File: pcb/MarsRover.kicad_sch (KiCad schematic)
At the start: 13 parts, among them M1 Vibrationsmotor L, M2 Vibrationsmotor R, Q1 AO3400A, Q2 AO3400A, U1 ESP32-DevKitC V4

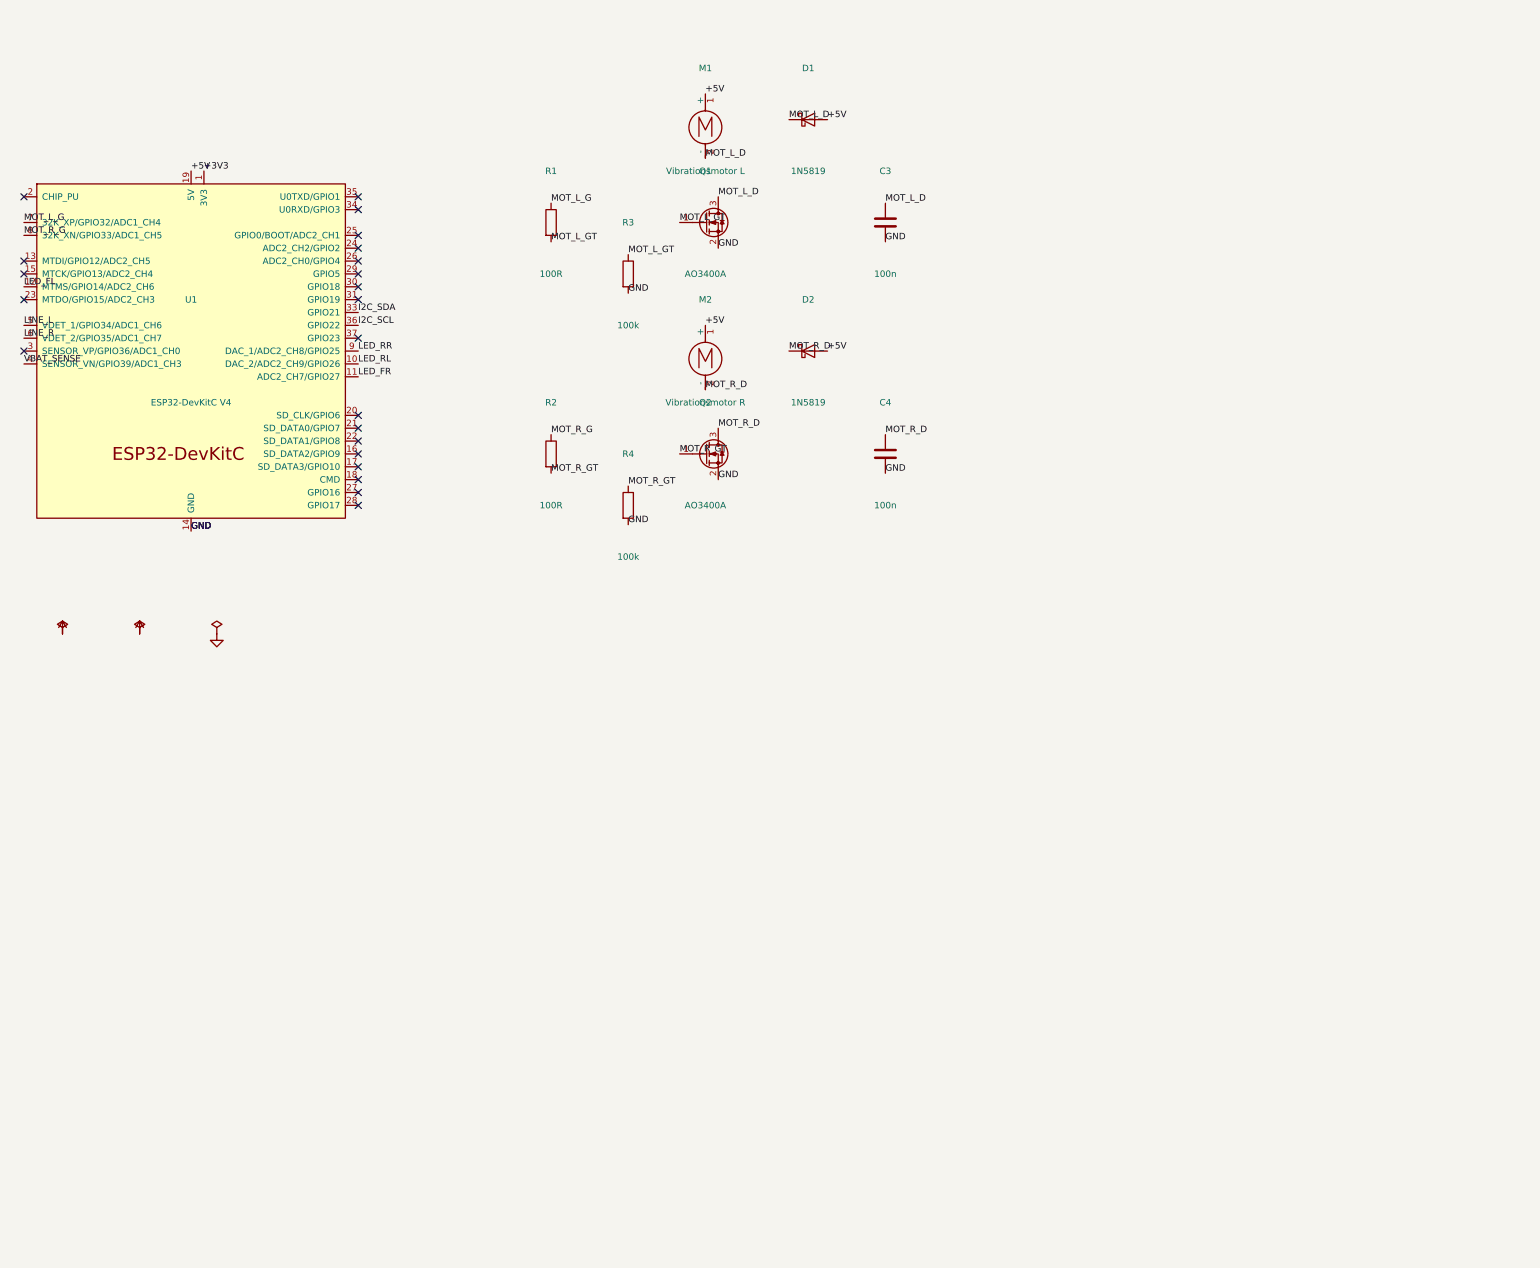
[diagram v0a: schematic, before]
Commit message: Schaltplan vollstaendig: 38 Bauteile, null ERC-Fehler
Stufe 2 ergaenzt: Liniensensoren mit Emitterfolger, vier Signal-LEDs mit
Vorwiderstaenden, beide I2C-Module als Steckverbinder, Ladeschaltung,
Schalter, Step-Up, Siebung und der optionale Spannungsteiler fuer die
Akkumessung.

106 Netzlabels, 23 Nicht-angeschlossen-Zeichen.
ERC: null Fehler, drei Warnungen, alle erklaert:
 * 2x lib_symbol_mismatch an den Dioden -- Folge des Aufloesens der
   Vererbung, kosmetisch, elektrisch ohne Wirkung
 * 1x USB_VBUS haengt allein, und das ist richtig: die USB-C-Buchse
   sitzt auf dem TP4056-Fertigmodul, nicht auf unserer Platine

Netzliste gegengeprueft: GND 29 Knoten, +5V 8, +3V3 7, I2C je 3,
die Motorzweige 4/3/2 wie entworfen.

Zur Frage nach einer interaktiven Loesung fuer den Schaltplan:
kipy bringt ein vollstaendiges schematic-Modul mit (create_items,
update_items, get_symbols, Commits), aber dessen Quelltext traegt
"versionadded: KiCad 11". Die mitgelieferten Protobuf-Definitionen sind
die von KiCad 10, daher fehlende Namen -- und die Gegenseite im
laufenden KiCad kennt die Befehle ohnehin nicht. Nicht ueberbrueckbar.
KiCad 11 wird fuer Februar 2027 erwartet; ein Wechsel hiesse Nightly,
und das Dateiformat waere eine Einbahnstrasse. Bleibt bei 10.

Co-Authored-By: Claude Opus 5 <noreply@anthropic.com>
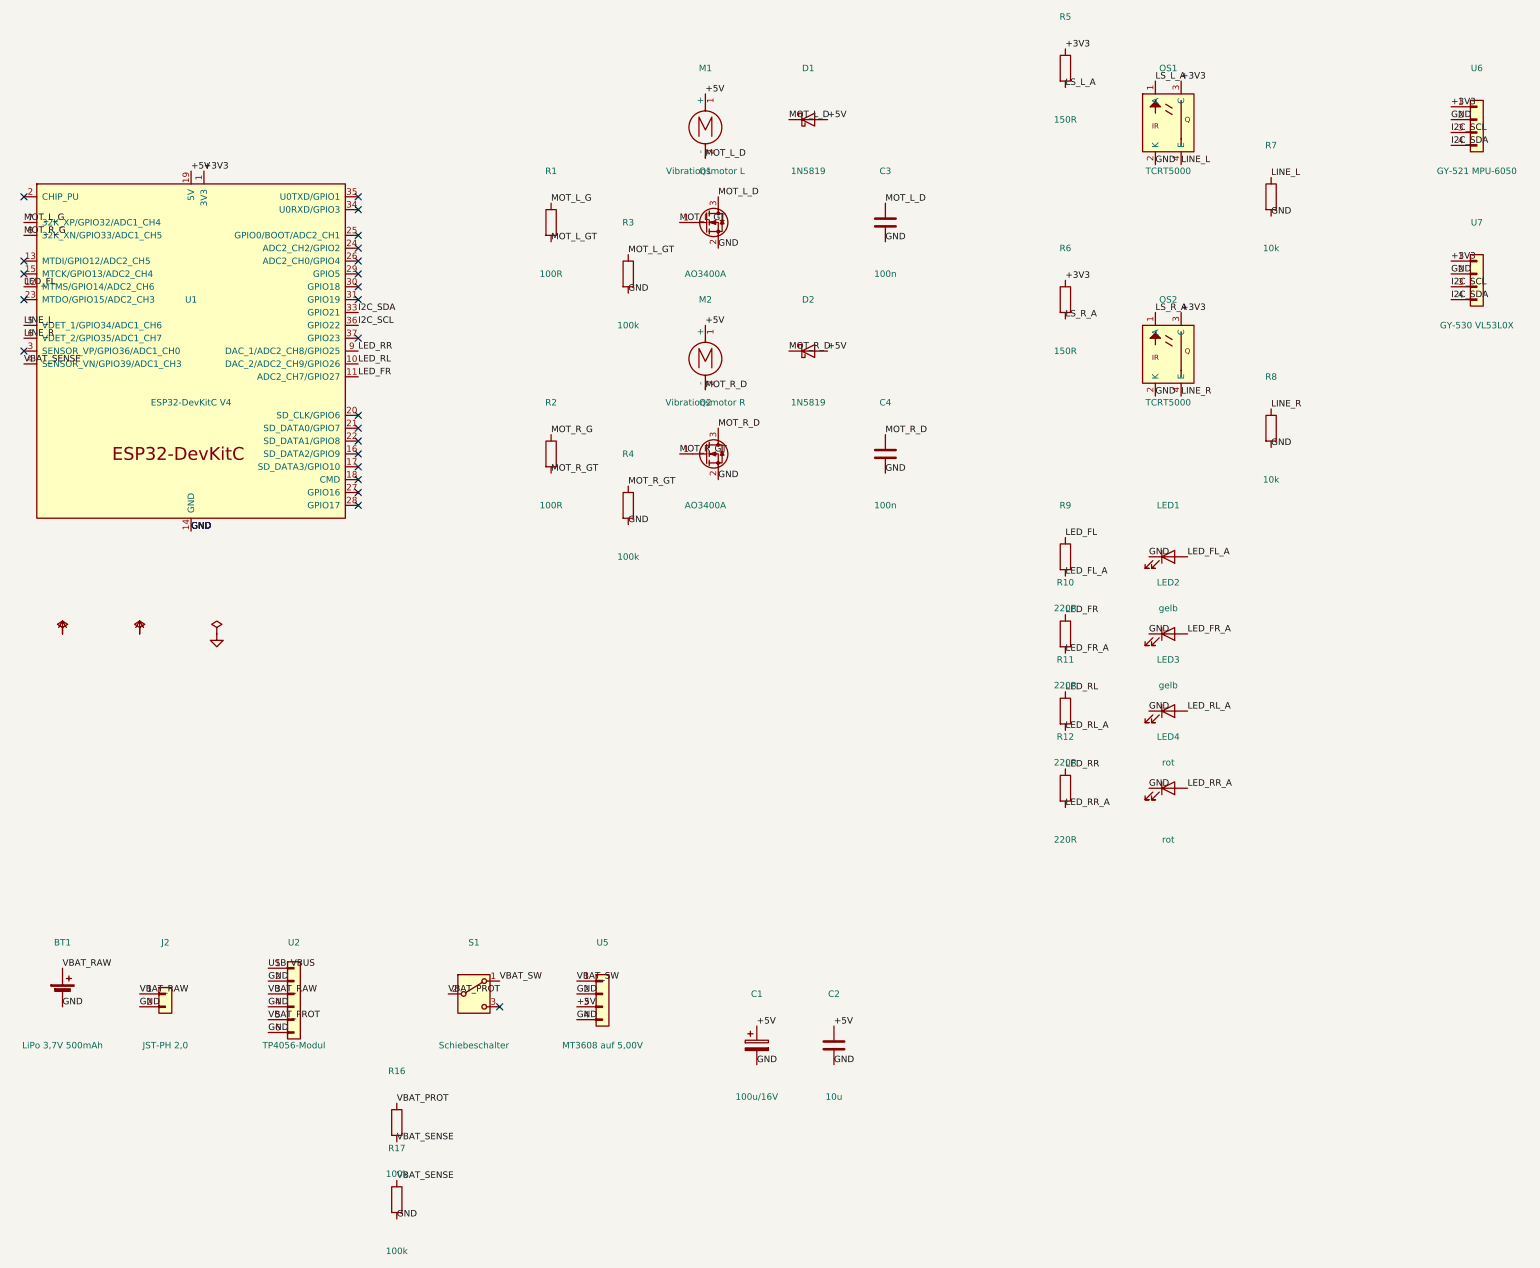
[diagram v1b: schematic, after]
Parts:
- added BT1: LiPo 3,7V 500mAh, symbol Device:Battery_Cell
- added C1: 100u/16V, symbol Device:C_Polarized
- added C2: 10u, symbol Device:C
- added J2: JST-PH 2,0, symbol Connector_Generic:Conn_01x02
- added LED1, LED2: gelb, symbol Device:LED
- added LED3, LED4: rot, symbol Device:LED
- added OS1, OS2: TCRT5000, symbol MarsRover:TCRT5000
- added R10, R11, R12, R9: 220R, symbol Device:R
- added R16, R17: 100k, symbol Device:R
- added R5, R6: 150R, symbol Device:R
- added R7, R8: 10k, symbol Device:R
- added S1: Schiebeschalter, symbol Switch:SW_SPDT
- added U2: TP4056-Modul, symbol Connector_Generic:Conn_01x06
- added U5: MT3608 auf 5,00V, symbol Connector_Generic:Conn_01x04
- added U6: GY-521 MPU-6050, symbol Connector_Generic:Conn_01x04
- added U7: GY-530 VL53L0X, symbol Connector_Generic:Conn_01x04
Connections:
- net +3V3: now also OS1.3 (C), OS2.3 (C), R5.1, R6.1, U6.1 (Pin_1), U7.1 (Pin_1)
- net +5V: now also C1.1, C2.1, U5.3 (Pin_3)
- net GND: now also BT1.2 (-), C1.2, C2.2, J2.2 (Pin_2), LED1.1 (K), LED2.1 (K), LED3.1 (K), LED4.1 (K), OS1.2 (K), OS2.2 (K), R17.2, R7.2, R8.2, U2.2 (Pin_2), U2.4 (Pin_4), U2.6 (Pin_6), U5.2 (Pin_2), U5.4 (Pin_4), U6.2 (Pin_2), U7.2 (Pin_2)
- net I2C_SCL: now also U6.3 (Pin_3), U7.3 (Pin_3)
- net I2C_SDA: now also U6.4 (Pin_4), U7.4 (Pin_4)
- net LED_FL: now also R9.1
- net LED_FR: now also R10.1
- net LED_RL: now also R11.1
- net LED_RR: now also R12.1
- net LINE_L: now also OS1.4 (E), R7.1
- net LINE_R: now also OS2.4 (E), R8.1
- net VBAT_SENSE: now also R16.2, R17.1
- new net LED_FL_A: LED1.2 (A), R9.2
- new net LED_FR_A: LED2.2 (A), R10.2
- new net LED_RL_A: LED3.2 (A), R11.2
- new net LED_RR_A: LED4.2 (A), R12.2
- new net LS_L_A: OS1.1 (A), R5.2
- new net LS_R_A: OS2.1 (A), R6.2
- new net USB_VBUS: U2.1 (Pin_1)
- new net VBAT_PROT: R16.1, S1.2 (B), U2.5 (Pin_5)
- new net VBAT_RAW: BT1.1 (+), J2.1 (Pin_1), U2.3 (Pin_3)
- new net VBAT_SW: S1.1 (A), U5.1 (Pin_1)
- no-connect marks 22 -> 23
